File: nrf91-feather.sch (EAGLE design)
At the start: 89 parts, among them J1 CON-USB-1050170001, J2 CON-HEADER-1X12-MALE-PIN, J3 CON-HEADER-1X16-MALE-PIN, J4 CON-1909763-1, J5 CON-SIM-104224-0820, J6 CON-S2B-PH-SM4-TB(LF)(SN), J7 CON-1909763-1, J9 CON-TC2030-MCP-NL, Q1 MOSFET-P-SC89, Q2 MOSFET-DUAL-COMP-SOT563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

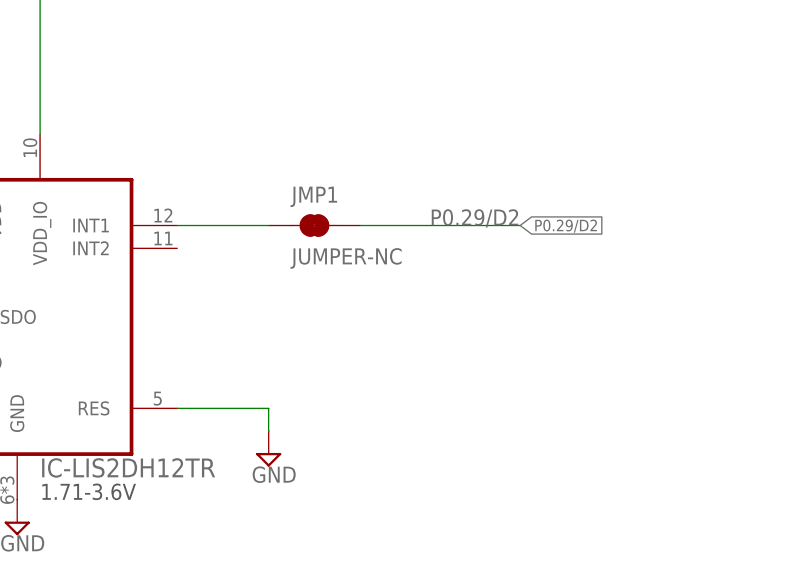
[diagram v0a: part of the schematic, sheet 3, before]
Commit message: Adding accelerometer INT2 pin connection.
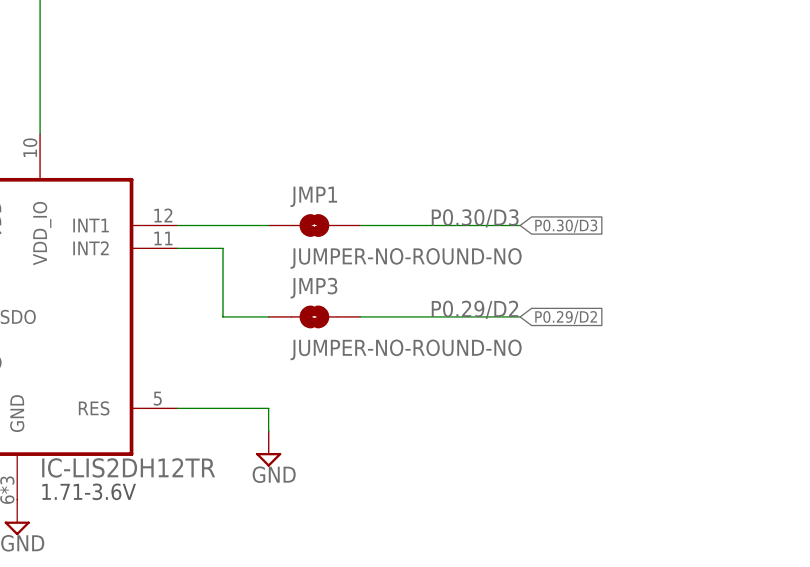
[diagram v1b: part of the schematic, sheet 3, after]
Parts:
- added JMP3: JUMPER-NO-ROUND-NO, wolff-den:JUMPER-NO-ROUND-NO
- JMP1: value JUMPER-NC -> JUMPER-NO-ROUND-NO; device wolff-den:JUMPER-NC -> wolff-den:JUMPER-NO-ROUND-NO
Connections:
- new net N$12: JMP3.1, U10.INT2
- net P0.29/D2: now also JMP3.2; no longer JMP1.2
- net P0.30/D3: now also JMP1.2
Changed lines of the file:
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@@
 <part name="ASSEMBLY1" library="wolff-den" library_urn="urn:adsk.eagle:library:6370453" deviceset="ASSY-COST" device="" package3d_urn="urn:adsk.eagle:package:10610054/3" technology="-NRF91-FEATHER"/>
 <part name="P+21" library="wolff-den" library_urn="urn:adsk.eagle:library:6370453" deviceset="VSYS" device=""/>
-<part name="JMP1" library="wolff-den" library_urn="urn:adsk.eagle:library:6370453" deviceset="JUMPER-NC" device="" package3d_urn="urn:adsk.eagle:package:24898428/1"/>
+<part name="JMP1" library="wolff-den" library_urn="urn:adsk.eagle:library:6370453" deviceset="JUMPER-NO" device="-ROUND-NO" package3d_urn="urn:adsk.eagle:package:24898427/1"/>
 <part name="JMP2" library="wolff-den" library_urn="urn:adsk.eagle:library:6370453" deviceset="JUMPER-3/1" device="" package3d_urn="urn:adsk.eagle:package:24898429/1"/>
 <part name="TP3" library="wolff-den" library_urn="urn:adsk.eagle:library:6370453" deviceset="TP" device="-1SIDE-1P0" package3d_urn="urn:adsk.eagle:package:24898411/1"/>
@@
 <part name="TP5" library="wolff-den" library_urn="urn:adsk.eagle:library:6370453" deviceset="TP" device="-1SIDE-1P0" package3d_urn="urn:adsk.eagle:package:24898411/1"/>
 <part name="TP6" library="wolff-den" library_urn="urn:adsk.eagle:library:6370453" deviceset="TP" device="-1SIDE-1P0" package3d_urn="urn:adsk.eagle:package:24898411/1"/>
+<part name="JMP3" library="wolff-den" library_urn="urn:adsk.eagle:library:6370453" deviceset="JUMPER-NO" device="-ROUND-NO" package3d_urn="urn:adsk.eagle:package:24898427/1"/>
 </parts>
 <sheets>
@@
 <attribute name="VALUE" x="337.82" y="99.06" size="1.778" layer="96" font="vector" align="top-left"/>
 </instance>
+<instance part="JMP3" gate="G$1" x="340.36" y="91.44" smashed="yes">
+<attribute name="NAME" x="337.82" y="93.98" size="1.778" layer="95" font="vector"/>
+<attribute name="VALUE" x="337.82" y="88.9" size="1.778" layer="96" font="vector" align="top-left"/>
+</instance>
 </instances>
 <busses>
@@
 </segment>
 </net>
-<net name="P0.29/D2" class="0">
+<net name="N$9" class="0">
+<segment>
+<pinref part="U10" gate="G$1" pin="INT1"/>
+<wire x1="325.12" y1="101.6" x2="335.28" y2="101.6" width="0.1524" layer="91"/>
+<pinref part="JMP1" gate="G$1" pin="1"/>
+</segment>
+</net>
+<net name="N$12" class="0">
 <segment>
-<wire x1="345.44" y1="101.6" x2="363.22" y2="101.6" width="0.1524" layer="91"/>
+<pinref part="JMP3" gate="G$1" pin="1"/>
+<wire x1="335.28" y1="91.44" x2="330.2" y2="91.44" width="0.1524" layer="91"/>
+<wire x1="330.2" y1="91.44" x2="330.2" y2="99.06" width="0.1524" layer="91"/>
+<pinref part="U10" gate="G$1" pin="INT2"/>
+<wire x1="330.2" y1="99.06" x2="325.12" y2="99.06" width="0.1524" layer="91"/>
+</segment>
+</net>
+<net name="P0.30/D3" class="0">
+<segment>
+<wire x1="363.22" y1="101.6" x2="345.44" y2="101.6" width="0.1524" layer="91"/>
 <label x="363.22" y="101.6" size="1.778" layer="95" rot="MR0"/>
-<label x="363.22" y="101.6" size="1.27" layer="95" xref="yes"/>
+<label x="363.22" y="101.6" size="1.27" layer="95" rot="MR180" xref="yes"/>
 <pinref part="JMP1" gate="G$1" pin="2"/>
 </segment>
 </net>
-<net name="N$9" class="0">
+<net name="P0.29/D2" class="0">
 <segment>
-<pinref part="U10" gate="G$1" pin="INT1"/>
-<wire x1="325.12" y1="101.6" x2="335.28" y2="101.6" width="0.1524" layer="91"/>
-<pinref part="JMP1" gate="G$1" pin="1"/>
+<wire x1="345.44" y1="91.44" x2="363.22" y2="91.44" width="0.1524" layer="91"/>
+<label x="363.22" y="91.44" size="1.778" layer="95" rot="MR0"/>
+<label x="363.22" y="91.44" size="1.27" layer="95" xref="yes"/>
+<pinref part="JMP3" gate="G$1" pin="2"/>
 </segment>
 </net>

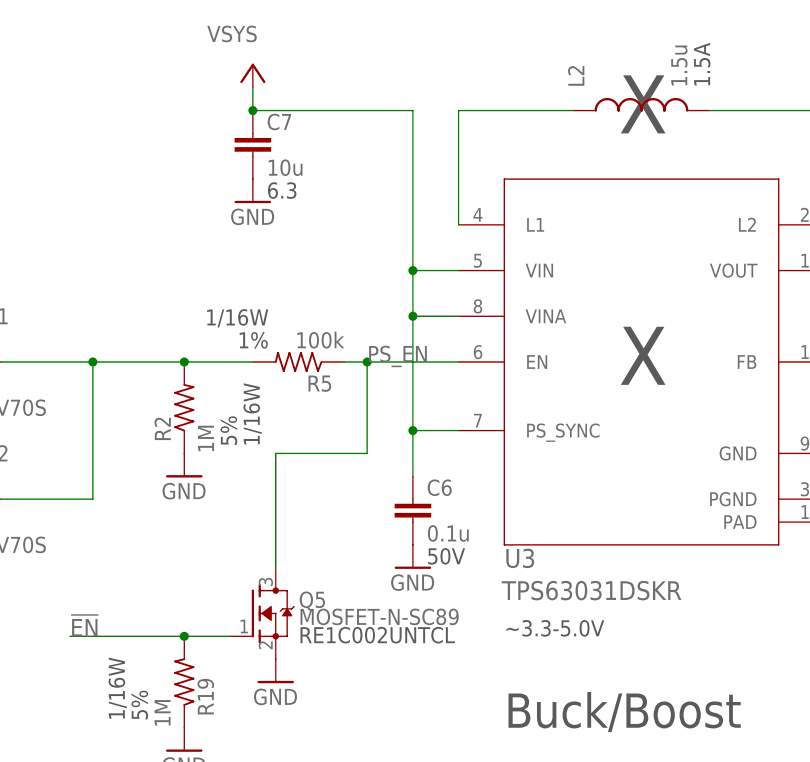
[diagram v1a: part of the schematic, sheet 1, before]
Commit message: Optimizing power layout
Changed:
* Created large power paths on middle layers (power an return)
* Pin7 on power supply chip to ground (power save mode/pfm enabled)
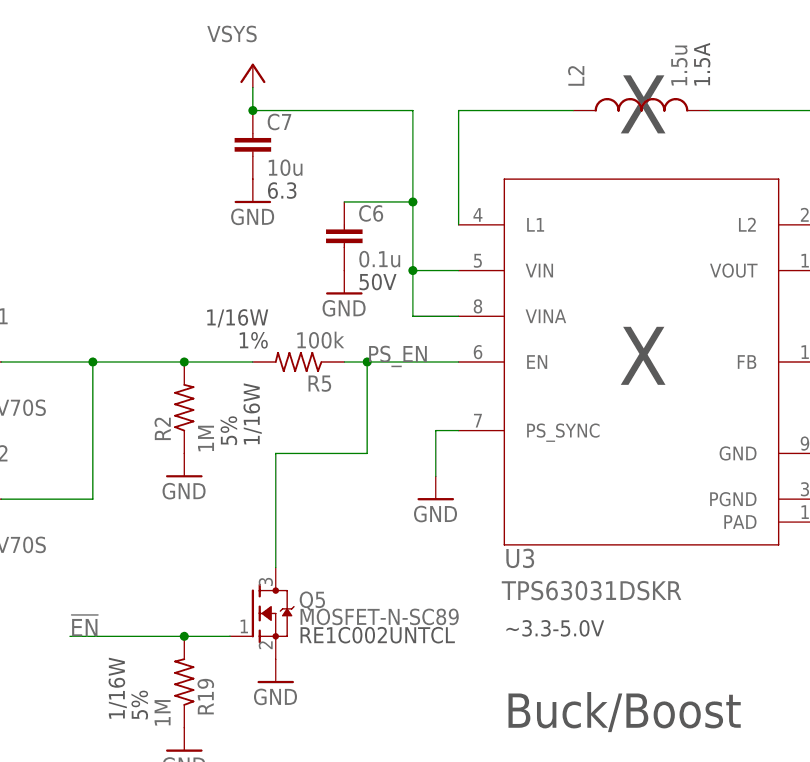
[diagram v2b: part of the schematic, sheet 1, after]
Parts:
- JMP1: value JUMPER-NO-ROUND-NO -> JUMPER-NC; device wolff-den:JUMPER-NO-ROUND-NO -> wolff-den:JUMPER-NC
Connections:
- net GND: now also U3.PS_SYNC
- net VSYS: no longer U3.PS_SYNC
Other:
- moved on the sheet: C6
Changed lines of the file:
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@@
 <part name="ASSEMBLY1" library="wolff-den" library_urn="urn:adsk.eagle:library:6370453" deviceset="ASSY-COST" device="" package3d_urn="urn:adsk.eagle:package:10610054/3" technology="-NRF91-FEATHER"/>
 <part name="P+21" library="wolff-den" library_urn="urn:adsk.eagle:library:6370453" deviceset="VSYS" device=""/>
-<part name="JMP1" library="wolff-den" library_urn="urn:adsk.eagle:library:6370453" deviceset="JUMPER-NO" device="-ROUND-NO" package3d_urn="urn:adsk.eagle:package:24898427/1"/>
+<part name="JMP1" library="wolff-den" library_urn="urn:adsk.eagle:library:6370453" deviceset="JUMPER-NC" device="" package3d_urn="urn:adsk.eagle:package:24898428/1"/>
 <part name="JMP2" library="wolff-den" library_urn="urn:adsk.eagle:library:6370453" deviceset="JUMPER-3/1" device="" package3d_urn="urn:adsk.eagle:package:24898429/1"/>
 <part name="TP3" library="wolff-den" library_urn="urn:adsk.eagle:library:6370453" deviceset="TP" device="-1SIDE-1P0" package3d_urn="urn:adsk.eagle:package:24898411/1"/>
@@
 <part name="TP6" library="wolff-den" library_urn="urn:adsk.eagle:library:6370453" deviceset="TP" device="-1SIDE-1P0" package3d_urn="urn:adsk.eagle:package:24898411/1"/>
 <part name="JMP3" library="wolff-den" library_urn="urn:adsk.eagle:library:6370453" deviceset="JUMPER-NO" device="-ROUND-NO" package3d_urn="urn:adsk.eagle:package:24898427/1"/>
+<part name="GND39" library="supply1" library_urn="urn:adsk.eagle:library:371" deviceset="GND" device=""/>
 </parts>
 <sheets>
@@
 <attribute name="VALUE" x="91.44" y="228.6" size="1.778" layer="96"/>
 </instance>
-<instance part="C6" gate="A" x="111.76" y="198.12" smashed="yes">
-<attribute name="NAME" x="113.284" y="198.501" size="1.778" layer="95"/>
-<attribute name="VALUE" x="113.284" y="193.421" size="1.778" layer="96"/>
-<attribute name="VOLTHIGH" x="113.284" y="190.881" size="1.778" layer="97"/>
-</instance>
-<instance part="GND21" gate="1" x="111.76" y="190.5" smashed="yes">
-<attribute name="VALUE" x="109.22" y="187.96" size="1.778" layer="96"/>
+<instance part="C6" gate="A" x="104.14" y="228.6" smashed="yes">
+<attribute name="NAME" x="105.664" y="228.981" size="1.778" layer="95"/>
+<attribute name="VALUE" x="105.664" y="223.901" size="1.778" layer="96"/>
+<attribute name="VOLTHIGH" x="105.664" y="221.361" size="1.778" layer="97"/>
+</instance>
+<instance part="GND21" gate="1" x="104.14" y="220.98" smashed="yes">
+<attribute name="VALUE" x="101.6" y="218.44" size="1.778" layer="96"/>
 </instance>
 <instance part="+3V2" gate="G$1" x="182.88" y="233.68" smashed="yes">
@@
 <instance part="JMP2" gate="G$1" x="43.18" y="228.6" smashed="yes" rot="MR0">
 <attribute name="NAME" x="40.64" y="228.981" size="1.778" layer="95" font="vector" rot="MR0"/>
+</instance>
+<instance part="GND39" gate="1" x="114.3" y="198.12" smashed="yes">
+<attribute name="VALUE" x="111.76" y="195.58" size="1.778" layer="96"/>
 </instance>
 </instances>
@@
 <pinref part="R19" gate="G$1" pin="1"/>
 <pinref part="GND46" gate="1" pin="GND"/>
+</segment>
+<segment>
+<pinref part="U3" gate="A" pin="PS_SYNC"/>
+<wire x1="116.84" y1="205.74" x2="114.3" y2="205.74" width="0.1524" layer="91"/>
+<wire x1="114.3" y1="205.74" x2="114.3" y2="200.66" width="0.1524" layer="91"/>
+<pinref part="GND39" gate="1" pin="GND"/>
 </segment>
 </net>
@@
 <junction x="93.98" y="241.3"/>
 <wire x1="116.84" y1="218.44" x2="111.76" y2="218.44" width="0.1524" layer="91"/>
-<wire x1="111.76" y1="218.44" x2="111.76" y2="205.74" width="0.1524" layer="91"/>
-<wire x1="111.76" y1="205.74" x2="116.84" y2="205.74" width="0.1524" layer="91"/>
 <pinref part="C6" gate="A" pin="1"/>
-<wire x1="111.76" y1="205.74" x2="111.76" y2="200.66" width="0.1524" layer="91"/>
-<junction x="111.76" y="205.74"/>
 <wire x1="111.76" y1="218.44" x2="111.76" y2="223.52" width="0.1524" layer="91"/>
-<junction x="111.76" y="218.44"/>
 <junction x="111.76" y="223.52"/>
 <wire x1="93.98" y1="241.3" x2="111.76" y2="241.3" width="0.1524" layer="91"/>
-<wire x1="111.76" y1="241.3" x2="111.76" y2="223.52" width="0.1524" layer="91"/>
+<wire x1="111.76" y1="241.3" x2="111.76" y2="231.14" width="0.1524" layer="91"/>
 <pinref part="U3" gate="A" pin="VIN"/>
-<pinref part="U3" gate="A" pin="PS_SYNC"/>
 <pinref part="U3" gate="A" pin="VINA"/>
-</segment>
-<segment>
+<wire x1="111.76" y1="231.14" x2="111.76" y2="223.52" width="0.1524" layer="91"/>
+<wire x1="104.14" y1="231.14" x2="111.76" y2="231.14" width="0.1524" layer="91"/>
+<junction x="111.76" y="231.14"/>
+</segment>
+<segment>

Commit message: Replacing U4 with 2.8V regulator.
Changed:
* U4 to MIC5365-2.8YC5-TR
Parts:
- U4: value POWER-SWITCH-MIC94092YC6 -> (none); device wolff-den:POWER-SWITCH-MIC94092YC6 -> wolff-den:POWER-VREG-EN-2.8V-150MA-SOT-353
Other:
- moved on the sheet: U4
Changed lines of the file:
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@@
 <part name="R19" library="wolff-den" library_urn="urn:adsk.eagle:library:6370453" deviceset="RES" device="-0402" package3d_urn="urn:adsk.eagle:package:19061974/3" technology="-1M-5%" value="1M"/>
 <part name="GND46" library="supply1" library_urn="urn:adsk.eagle:library:371" deviceset="GND" device=""/>
-<part name="U4" library="wolff-den" library_urn="urn:adsk.eagle:library:6370453" deviceset="POWER-SWITCH" device="-MIC94092YC6" package3d_urn="urn:adsk.eagle:package:5807345/9"/>
+<part name="U4" library="wolff-den" library_urn="urn:adsk.eagle:library:6370453" deviceset="POWER-VREG-EN" device="-SOT-353" package3d_urn="urn:adsk.eagle:package:19061981/1" technology="-2.8V-150MA"/>
 <part name="GND27" library="supply1" library_urn="urn:adsk.eagle:library:371" deviceset="GND" device=""/>
 <part name="C2" library="wolff-den" library_urn="urn:adsk.eagle:library:6370453" deviceset="CAP" device="-0402" package3d_urn="urn:adsk.eagle:package:7419912/5" technology="-15P-50V" value="15p">

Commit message: Comparing and fixing U3 connections
Changed:
* U3.8 should not be connected to VSYS. Now the same as a few reference designs i've seen.
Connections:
- new net N$14: C6.1, U3.VINA
- net VSYS: no longer C6.1, U3.VINA
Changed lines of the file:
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@@
 </segment>
 <segment>
-<wire x1="116.84" y1="223.52" x2="111.76" y2="223.52" width="0.1524" layer="91"/>
+<wire x1="116.84" y1="223.52" x2="114.3" y2="223.52" width="0.1524" layer="91"/>
 <wire x1="93.98" y1="241.3" x2="93.98" y2="243.84" width="0.1524" layer="91"/>
 <pinref part="P+5" gate="G$2" pin="VSYS"/>
 <pinref part="C7" gate="A" pin="1"/>
 <junction x="93.98" y="241.3"/>
-<wire x1="116.84" y1="218.44" x2="111.76" y2="218.44" width="0.1524" layer="91"/>
-<pinref part="C6" gate="A" pin="1"/>
-<wire x1="111.76" y1="218.44" x2="111.76" y2="223.52" width="0.1524" layer="91"/>
-<junction x="111.76" y="223.52"/>
-<wire x1="93.98" y1="241.3" x2="111.76" y2="241.3" width="0.1524" layer="91"/>
-<wire x1="111.76" y1="241.3" x2="111.76" y2="231.14" width="0.1524" layer="91"/>
+<wire x1="93.98" y1="241.3" x2="114.3" y2="241.3" width="0.1524" layer="91"/>
 <pinref part="U3" gate="A" pin="VIN"/>
-<pinref part="U3" gate="A" pin="VINA"/>
-<wire x1="111.76" y1="231.14" x2="111.76" y2="223.52" width="0.1524" layer="91"/>
-<wire x1="104.14" y1="231.14" x2="111.76" y2="231.14" width="0.1524" layer="91"/>
-<junction x="111.76" y="231.14"/>
+<wire x1="114.3" y1="223.52" x2="114.3" y2="241.3" width="0.1524" layer="91"/>
 </segment>
 <segment>
@@
 </segment>
 </net>
+<net name="N$14" class="0">
+<segment>
+<pinref part="U3" gate="A" pin="VINA"/>
+<wire x1="116.84" y1="218.44" x2="111.76" y2="218.44" width="0.1524" layer="91"/>
+<pinref part="C6" gate="A" pin="1"/>
+<wire x1="104.14" y1="231.14" x2="111.76" y2="231.14" width="0.1524" layer="91"/>
+<wire x1="111.76" y1="231.14" x2="111.76" y2="218.44" width="0.1524" layer="91"/>
+</segment>
+</net>

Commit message: Undo changing U4 to LDO. Needs to stay as a load switch.
Changed:
* U4 back to the original part.
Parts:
- U4: value (none) -> POWER-SWITCH-MIC94092YC6; device wolff-den:POWER-VREG-EN-2.8V-150MA-SOT-353 -> wolff-den:POWER-SWITCH-MIC94092YC6
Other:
- note added: "TODO: * Larger caps * Test LDO for LNA"
- moved on the sheet: U4
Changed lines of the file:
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@@
 <part name="R19" library="wolff-den" library_urn="urn:adsk.eagle:library:6370453" deviceset="RES" device="-0402" package3d_urn="urn:adsk.eagle:package:19061974/3" technology="-1M-5%" value="1M"/>
 <part name="GND46" library="supply1" library_urn="urn:adsk.eagle:library:371" deviceset="GND" device=""/>
-<part name="U4" library="wolff-den" library_urn="urn:adsk.eagle:library:6370453" deviceset="POWER-VREG-EN" device="-SOT-353" package3d_urn="urn:adsk.eagle:package:19061981/1" technology="-2.8V-150MA"/>
+<part name="U4" library="wolff-den" library_urn="urn:adsk.eagle:library:6370453" deviceset="POWER-SWITCH" device="-MIC94092YC6" package3d_urn="urn:adsk.eagle:package:5807345/9"/>
 <part name="GND27" library="supply1" library_urn="urn:adsk.eagle:library:371" deviceset="GND" device=""/>
 <part name="C2" library="wolff-den" library_urn="urn:adsk.eagle:library:6370453" deviceset="CAP" device="-0402" package3d_urn="urn:adsk.eagle:package:7419912/5" technology="-15P-50V" value="15p">
@@
 <wire x1="309.70276875" y1="15.25115" x2="309.73323125" y2="15.328340625" width="0" layer="97" curve="-87.5"/>
 <text x="38.1" y="5.08" size="3.81" layer="97">Some schematic symbols from Sparkfun</text>
+<text x="195.58" y="218.44" size="1.778" layer="91">TODO:
+* Larger caps
+* Test LDO for LNA</text>
 </plain>
 <instances>
